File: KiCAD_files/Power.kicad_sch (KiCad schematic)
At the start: 44 parts, among them J101 Wago 6 contacts, P101 Power2, U101 AMC1311, U102 MCP6486UT-E/LT, U103 MCP6486UT-E/LT, U104 ACS723LLCTR-20AB

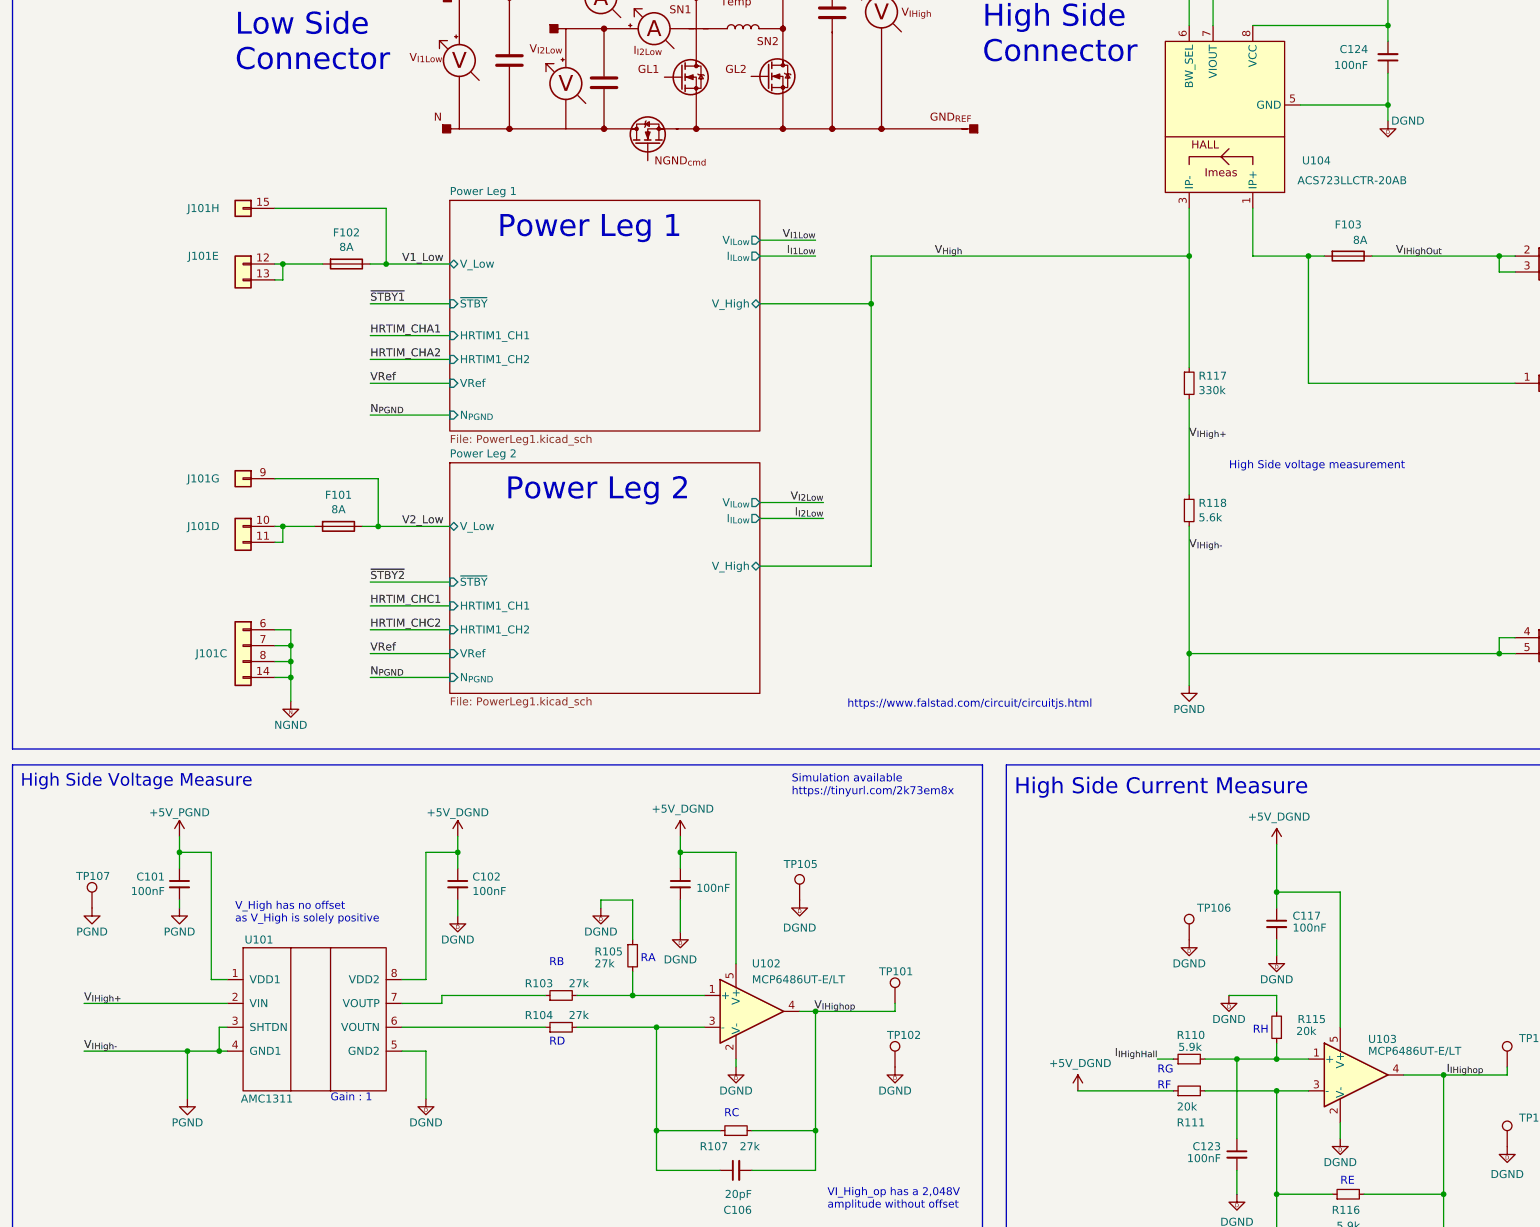
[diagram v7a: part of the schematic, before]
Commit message: Schematic OK, (waiting OPTOCOUPLER FIX)
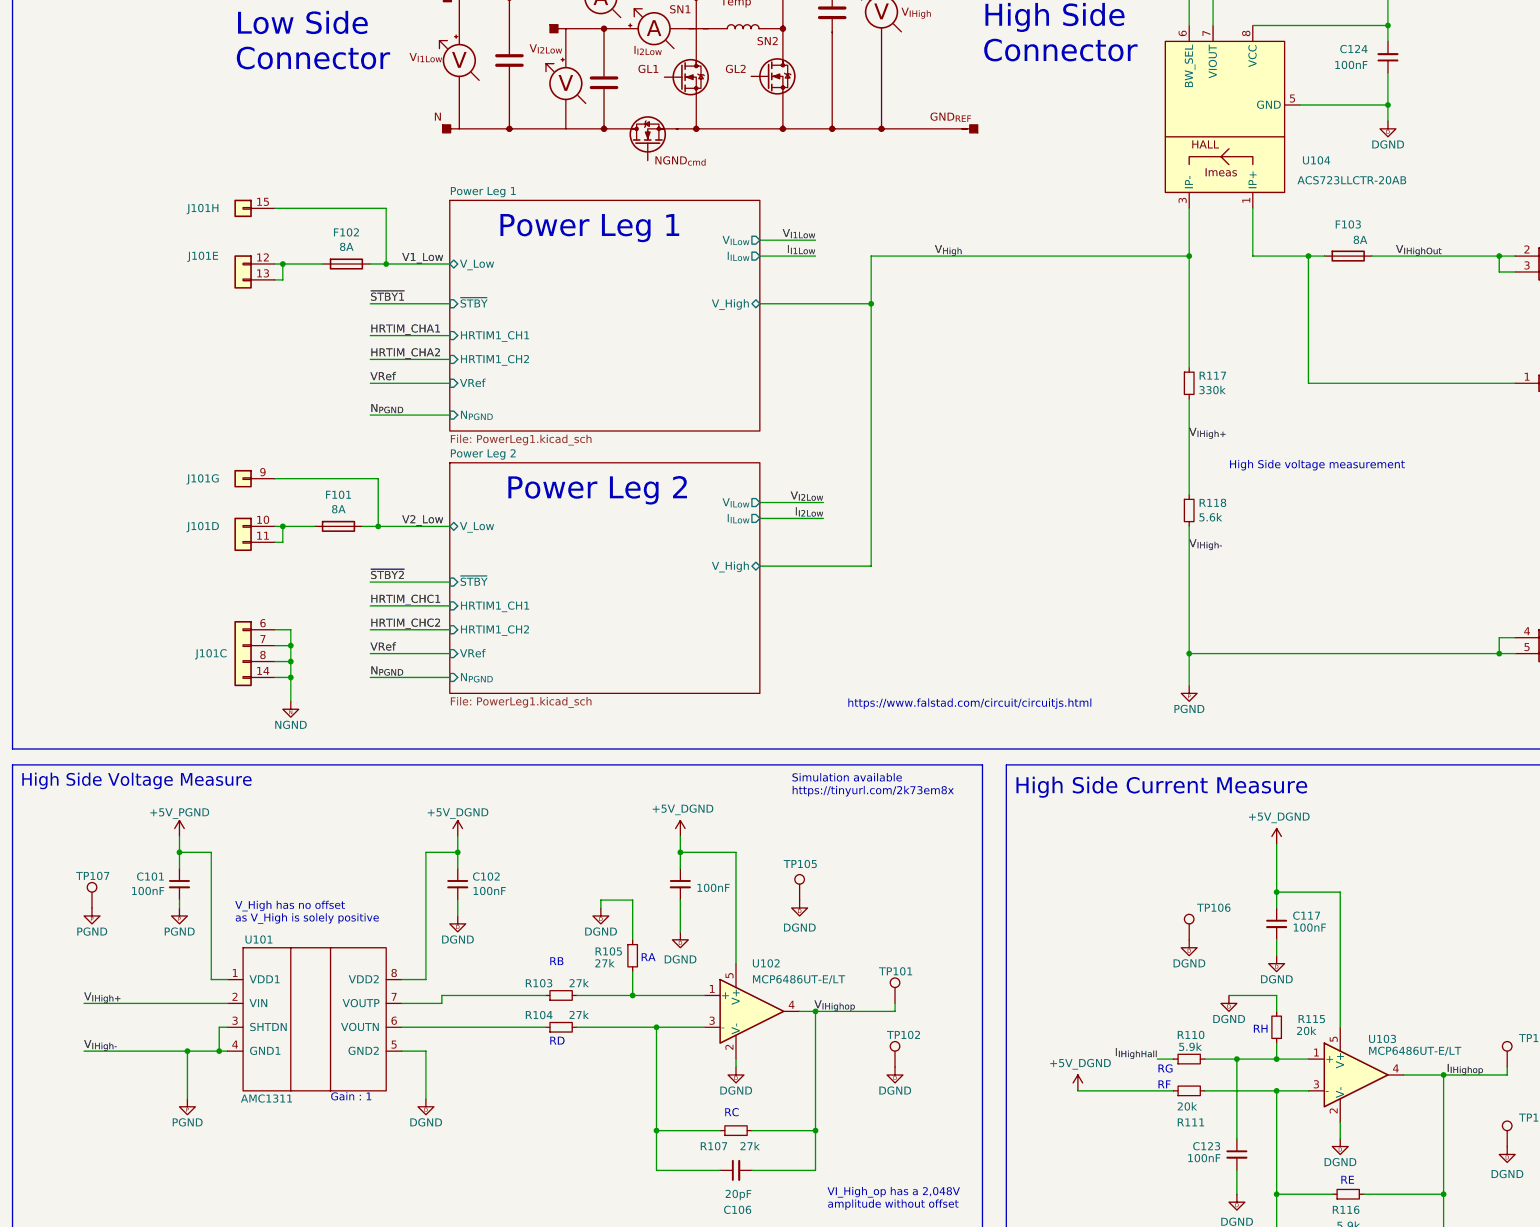
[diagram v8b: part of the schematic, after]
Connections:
- net +5P is gone; now on net +5V_PGND: C101.1, U101.1 (VDD1)
- net +5VD is gone; now on net +5V_DGND: C102.1, C103.1, C117.1, C124.2, R111.1, U101.8 (VDD2), U102.5 (V+), U103.5 (V+), U104.6 (BW_SEL), U104.8 (VCC)
- net GND renamed PGND
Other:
- title: Power Board Scheme -> TWIST 1.4
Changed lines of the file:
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@@
   (paper "A3")
   (title_block
-    (title "Power Board Scheme")
+    (title "TWIST 1.4")
     (date "2022-06-10")
     (company "https://gitlab.laas.fr/owntech/1leg/-/tree/V1.1.1/KiCAD_files")
@@
     )
   )
-  (symbol (lib_name "+5VD_1") (lib_id "power:+5VD") (at 223.52 181.61 0) (unit 1)
-    (in_bom yes) (on_board yes) (dnp no)
+  (symbol (lib_id "Symbols:+5V_DGND") (at 223.52 181.61 0) (unit 1)
+    (in_bom no) (on_board no) (dnp no)
     (property "Reference" "#PWR0116" (at 223.52 185.42 0)
       (effects (font (size 1.27 1.27)) hide)
@@
       (effects (font (size 1.27 1.27)))
     )
-    (property "Footprint" "" (at 223.52 181.61 0)
+    (property "Footprint" "" (at 226.695 179.07 0)
       (effects (font (size 1.27 1.27)) hide)
     )
-    (property "Datasheet" "" (at 223.52 181.61 0)
+    (property "Datasheet" "" (at 226.695 179.07 0)
       (effects (font (size 1.27 1.27)) hide)
     )
@@
     )
   )
-  (symbol (lib_id "power:GND") (at 209.55 156.21 0) (unit 1)
+  (symbol (lib_id "Symbols:PGND") (at 209.55 156.21 0) (unit 1)
     (in_bom yes) (on_board yes) (dnp no)
     (property "Reference" "#PWR0113" (at 209.55 162.56 0)
@@
     )
   )
-  (symbol (lib_id "power:GND") (at 48.26 191.77 0) (unit 1)
+  (symbol (lib_id "Symbols:PGND") (at 48.26 191.77 0) (unit 1)
     (in_bom yes) (on_board yes) (dnp no)
     (property "Reference" "#PWR0103" (at 48.26 198.12 0)
@@
     )
   )
-  (symbol (lib_id "power:GND") (at 49.53 222.25 0) (unit 1)
+  (symbol (lib_id "Symbols:PGND") (at 49.53 222.25 0) (unit 1)
     (in_bom yes) (on_board yes) (dnp no)
     (property "Reference" "#PWR0104" (at 49.53 228.6 0)
@@
     )
   )
-  (symbol (lib_id "power:+5P") (at 48.26 180.34 0) (unit 1)
-    (in_bom yes) (on_board yes) (dnp no)
+  (symbol (lib_id "Symbols:+5V_PGND") (at 48.26 180.34 0) (unit 1)
+    (in_bom no) (on_board no) (dnp no)
     (property "Reference" "#PWR0102" (at 48.26 184.15 0)
       (effects (font (size 1.27 1.27)) hide)
@@
       (effects (font (size 1.27 1.27)))
     )
-    (property "Footprint" "" (at 48.26 180.34 0)
+    (property "Footprint" "" (at 51.435 177.8 0)
       (effects (font (size 1.27 1.27)) hide)
     )
-    (property "Datasheet" "" (at 48.26 180.34 0)
+    (property "Datasheet" "" (at 51.435 177.8 0)
       (effects (font (size 1.27 1.27)) hide)
     )
@@
     )
   )
-  (symbol (lib_name "+5VD_1") (lib_id "power:+5VD") (at 191.77 220.98 0) (unit 1)
-    (in_bom yes) (on_board yes) (dnp no)
+  (symbol (lib_id "Symbols:+5V_DGND") (at 191.77 220.98 0) (unit 1)
+    (in_bom no) (on_board no) (dnp no)
     (property "Reference" "#PWR0114" (at 191.77 224.79 0)
       (effects (font (size 1.27 1.27)) hide)
@@
       (effects (font (size 1.27 1.27)))
     )
-    (property "Footprint" "" (at 191.77 220.98 0)
+    (property "Footprint" "" (at 194.945 218.44 0)
       (effects (font (size 1.27 1.27)) hide)
     )
-    (property "Datasheet" "" (at 191.77 220.98 0)
+    (property "Datasheet" "" (at 194.945 218.44 0)
       (effects (font (size 1.27 1.27)) hide)
     )
@@
     )
   )
-  (symbol (lib_name "+5VD_2") (lib_id "power:+5VD") (at 241.3 43.18 0) (unit 1)
-    (in_bom yes) (on_board yes) (dnp no)
+  (symbol (lib_id "Symbols:+5V_DGND") (at 241.3 43.18 0) (unit 1)
+    (in_bom no) (on_board no) (dnp no)
     (property "Reference" "#PWR0120" (at 241.3 46.99 0)
       (effects (font (size 1.27 1.27)) hide)
@@
       (effects (font (size 1.27 1.27)))
     )
-    (property "Footprint" "" (at 241.3 43.18 0)
+    (property "Footprint" "" (at 244.475 40.64 0)
       (effects (font (size 1.27 1.27)) hide)
     )
-    (property "Datasheet" "" (at 241.3 43.18 0)
+    (property "Datasheet" "" (at 244.475 40.64 0)
       (effects (font (size 1.27 1.27)) hide)
     )
@@
     )
   )
-  (symbol (lib_name "+5VD_4") (lib_id "power:+5VD") (at 92.71 180.34 0) (mirror y) (unit 1)
-    (in_bom yes) (on_board yes) (dnp no)
+  (symbol (lib_id "Symbols:+5V_DGND") (at 92.71 180.34 0) (mirror y) (unit 1)
+    (in_bom no) (on_board no) (dnp no)
     (property "Reference" "#PWR0105" (at 92.71 184.15 0)
       (effects (font (size 1.27 1.27)) hide)
@@
       (effects (font (size 1.27 1.27)))
     )
-    (property "Footprint" "" (at 92.71 180.34 0)
+    (property "Footprint" "" (at 89.535 177.8 0)
       (effects (font (size 1.27 1.27)) hide)
     )
-    (property "Datasheet" "" (at 92.71 180.34 0)
+    (property "Datasheet" "" (at 89.535 177.8 0)
       (effects (font (size 1.27 1.27)) hide)
     )
@@
     )
   )
-  (symbol (lib_name "+5VD_2") (lib_id "power:+5VD") (at 209.55 43.18 0) (unit 1)
-    (in_bom yes) (on_board yes) (dnp no)
+  (symbol (lib_id "Symbols:+5V_DGND") (at 209.55 43.18 0) (unit 1)
+    (in_bom no) (on_board no) (dnp no)
     (property "Reference" "#PWR0119" (at 209.55 46.99 0)
       (effects (font (size 1.27 1.27)) hide)
@@
       (effects (font (size 1.27 1.27)))
     )
-    (property "Footprint" "" (at 209.55 43.18 0)
+    (property "Footprint" "" (at 212.725 40.64 0)
       (effects (font (size 1.27 1.27)) hide)
     )
-    (property "Datasheet" "" (at 209.55 43.18 0)
+    (property "Datasheet" "" (at 212.725 40.64 0)
       (effects (font (size 1.27 1.27)) hide)
     )
@@
     )
   )
-  (symbol (lib_id "power:GND") (at 34.29 191.77 0) (unit 1)
+  (symbol (lib_id "Symbols:PGND") (at 34.29 191.77 0) (unit 1)
     (in_bom yes) (on_board yes) (dnp no)
     (property "Reference" "#PWR0142" (at 34.29 198.12 0)
@@
       (effects (font (size 1.27 1.27)) hide)
     )
-    (property "Value" "DGND" (at 244.475 66.04 0)
+    (property "Value" "DGND" (at 241.3 69.85 0)
       (effects (font (size 1.27 1.27)))
     )
@@
     )
   )
-  (symbol (lib_name "+5VD_3") (lib_id "power:+5VD") (at 128.27 180.34 0) (unit 1)
-    (in_bom yes) (on_board yes) (dnp no)
+  (symbol (lib_id "Symbols:+5V_DGND") (at 128.27 180.34 0) (unit 1)
+    (in_bom no) (on_board no) (dnp no)
     (property "Reference" "#PWR0110" (at 128.27 184.15 0)
       (effects (font (size 1.27 1.27)) hide)
@@
       (effects (font (size 1.27 1.27)))
     )
-    (property "Footprint" "" (at 128.27 180.34 0)
+    (property "Footprint" "" (at 131.445 177.8 0)
       (effects (font (size 1.27 1.27)) hide)
     )
-    (property "Datasheet" "" (at 128.27 180.34 0)
+    (property "Datasheet" "" (at 131.445 177.8 0)
       (effects (font (size 1.27 1.27)) hide)
     )
